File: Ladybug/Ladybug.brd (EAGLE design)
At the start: 42.3 x 50.8 mm, 8 parts

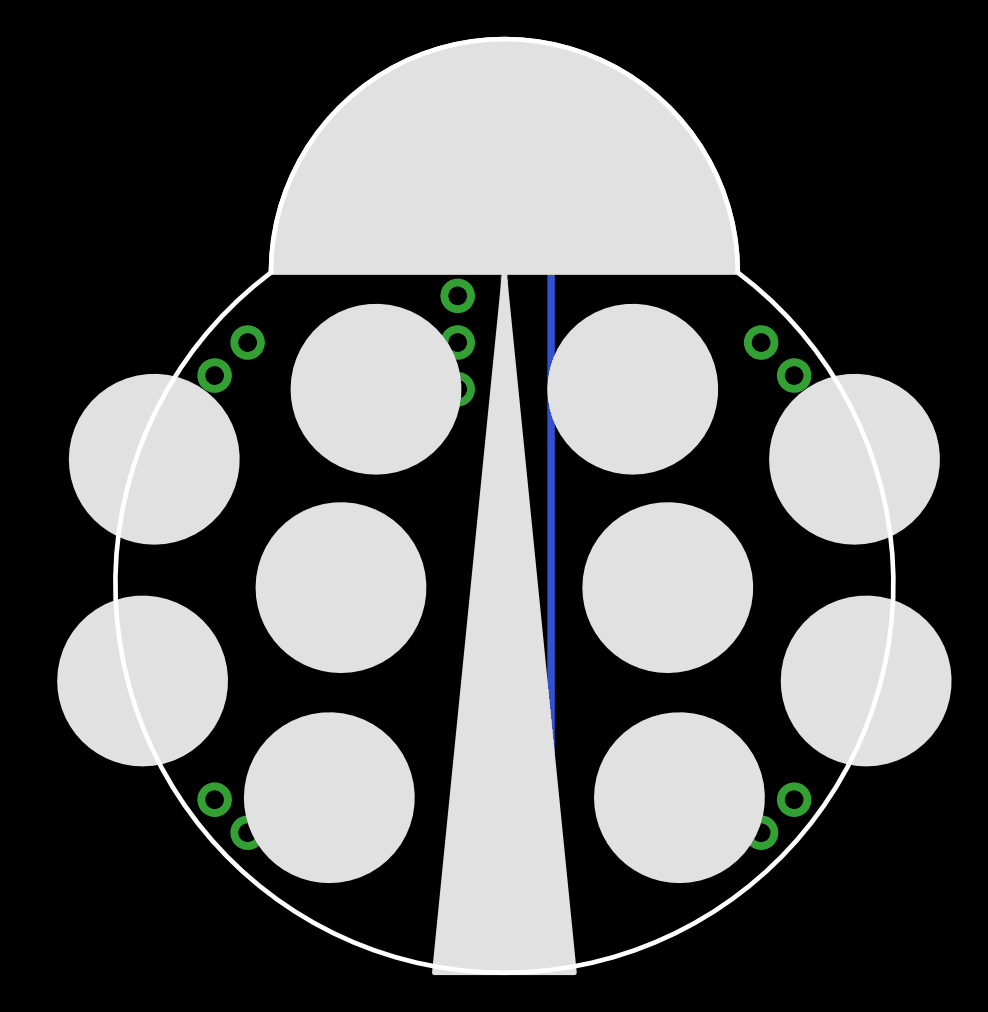
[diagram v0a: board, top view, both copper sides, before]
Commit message: Modifieg silkscreen decorations
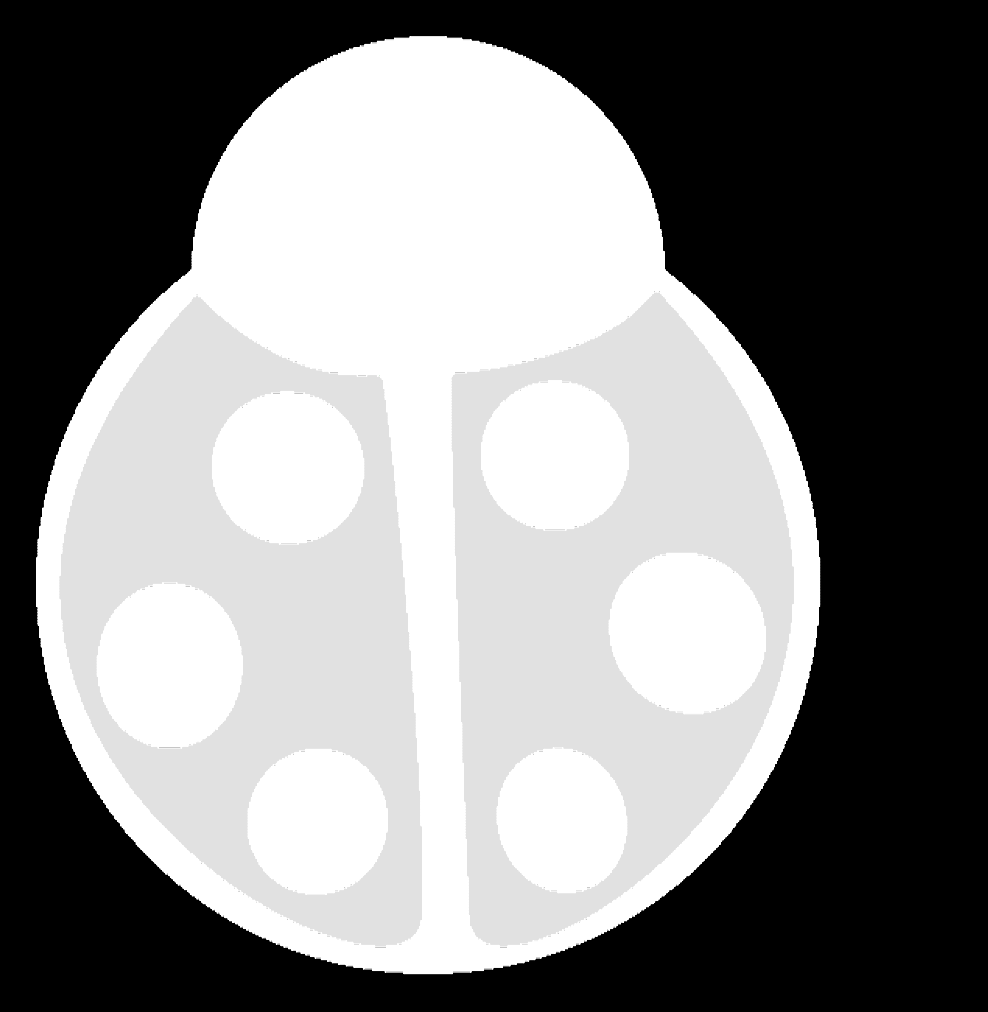
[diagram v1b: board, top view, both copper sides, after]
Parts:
- moved J1 4.24 mm to (23.7, 2.71)
- moved J2 4.24 mm to (7.20, 34.5)
- moved J5 4.24 mm to (7.20, 7.79)
- moved BATT 4.24 mm to (21.2, 6.52)
- moved J3 4.24 mm to (35.1, 34.5)
- moved J4 4.24 mm to (35.1, 7.79)
- moved J6 4.24 mm to (18.6, 31.9)
- moved R1 4.24 mm to (21.2, 47.8)
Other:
- board size 42.3 x 50.8 mm -> 42.6 x 51 mm
